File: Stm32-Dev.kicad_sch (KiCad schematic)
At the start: 1 part, among them U1 STM32F405RGTx

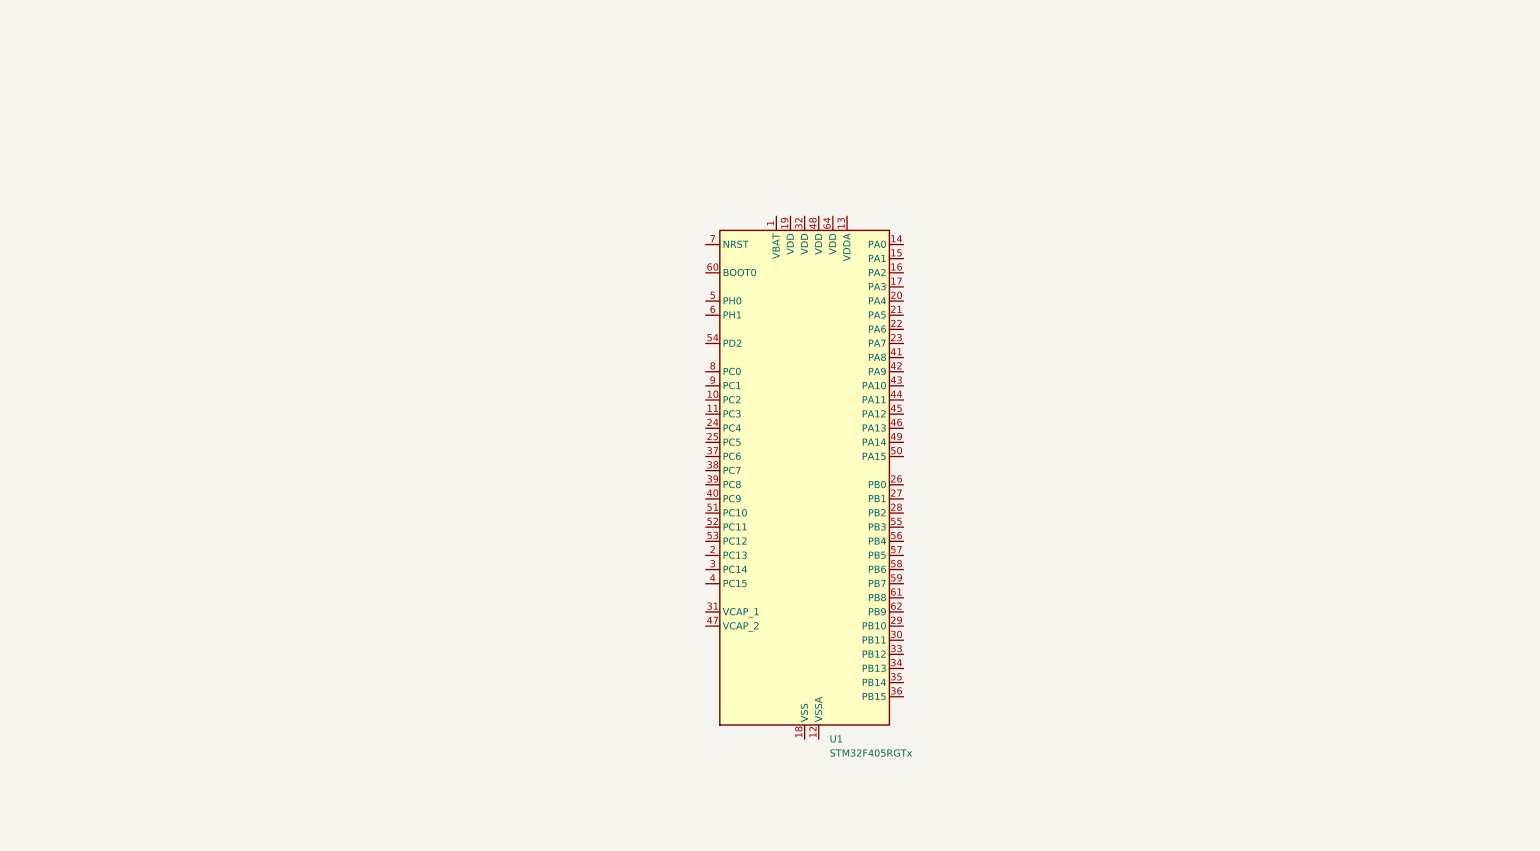
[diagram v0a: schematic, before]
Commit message: Basic MCU Setup
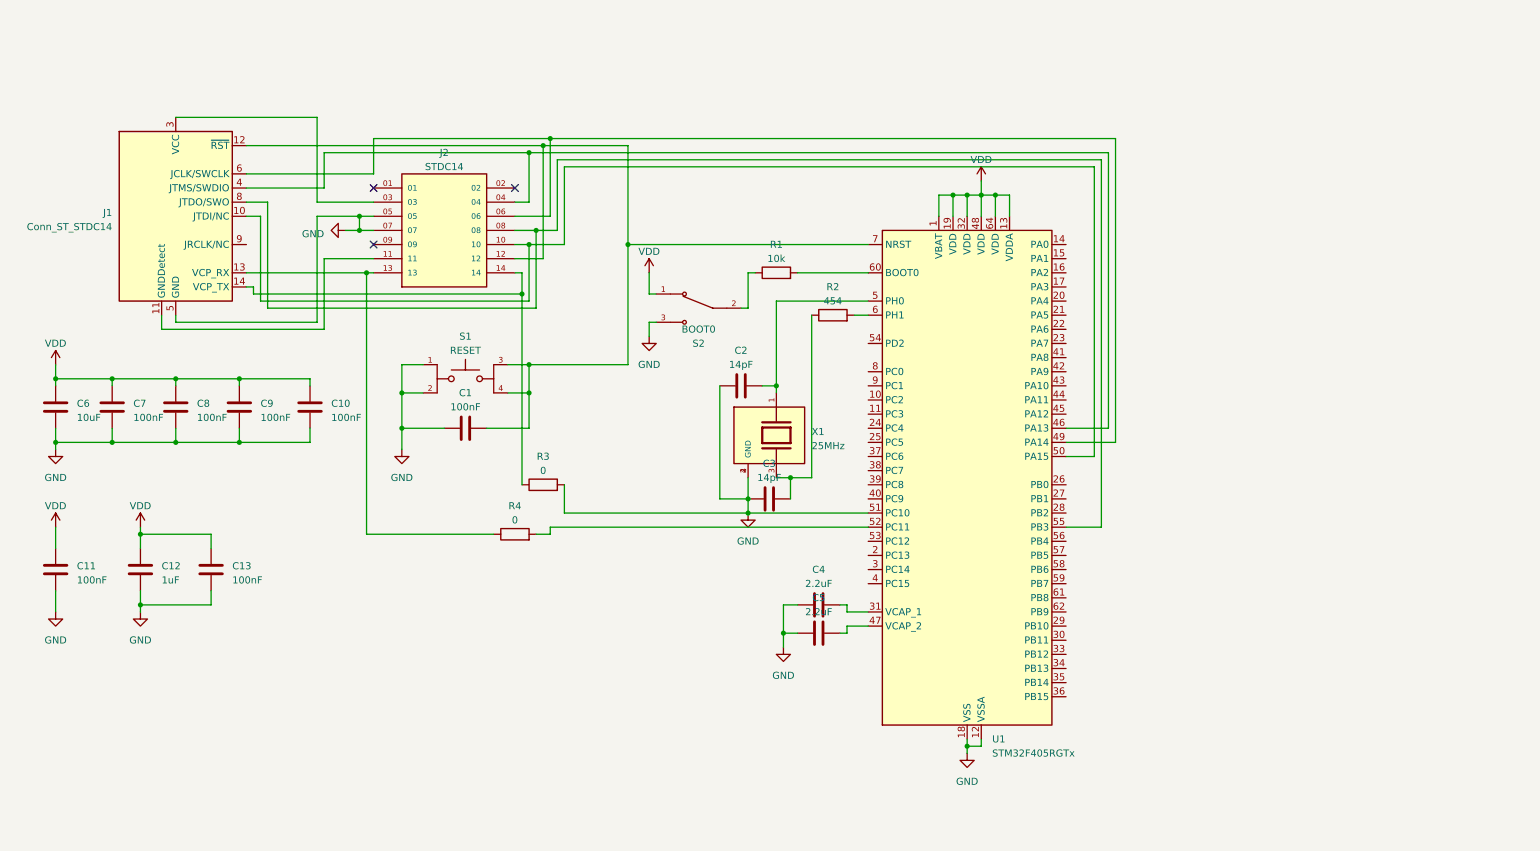
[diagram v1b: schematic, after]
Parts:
- added C1, C10, C11, C13, C7, C8, C9: 100nF, Capacitor_SMD:C_0805_2012Metric, symbol Device:C
- added C12: 1uF, Capacitor_SMD:C_0805_2012Metric, symbol Device:C
- added C2, C3: 14pF, Capacitor_SMD:C_0805_2012Metric, symbol Device:C
- added C4, C5: 2.2uF, Capacitor_SMD:C_0805_2012Metric, symbol Device:C
- added C6: 10uF, Capacitor_SMD:C_0805_2012Metric, symbol Device:C
- added J1: Conn_ST_STDC14, symbol Connector:Conn_ST_STDC14
- added J2: STDC14, SAMTEC_FTSH-107-01-L-DV-K, symbol FTSH-107-01-L-DV-K:FTSH-107-01-L-DV-K
- added R1: 10k, Resistor_SMD:R_0805_2012Metric, symbol Device:R
- added R2: 454, symbol Device:R
- added R3, R4: 0, symbol Device:R
- added S1: RESET, SW_TL3301AF160QG, symbol TL3301AF160QG:TL3301AF160QG
- added S2: BOOT0, Button_Switch_THT:SW_E-Switch_EG1224_SPDT_Angled, symbol EG1215AA:EG1215AA
- added X1: 25MHz, XTAL_ABM10W-25.0000MHZ-7-D1X-T3, symbol ABM10W-25.0000MHZ-7-D1X-T3:ABM10W-25.0000MHZ-7-D1X-T3
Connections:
- net VDD: now reaches U1.1 (VBAT)
- net VDD: now also U1.13 (VDDA), U1.19 (VDD), U1.32 (VDD), U1.48 (VDD), U1.64 (VDD), C10.1, C11.1, C12.1, C13.1, C6.1, C7.1, C8.1, C9.1, S2.1
- net GND: now reaches U1.12 (VSSA)
- net GND: now also U1.18 (VSS), U1.51 (PC10), U1.63 (VSS), C1.2, C10.2, C11.2, C12.2, C13.2, C2.2, C3.2, C4.2, C5.2, C6.2, C7.2, C8.2, C9.2, J1.5 (GND), J1.7 (GND), J2.05, J2.07, R3.2, S1.1, S1.2, S2.3, X1.2 (GND), X1.4 (GND)
- net at U1.31 (VCAP_1): now also C4.1
- net at U1.46 (PA13): now also J1.4 (JTMS/SWDIO), J2.04
- net at U1.47 (VCAP_2): now also C5.1
- net at U1.49 (PA14): now also J1.6 (JCLK/SWCLK), J2.06
- net at U1.5 (PH0): now also C2.1, X1.1
- net at U1.50 (PA15): now also J1.10 (JTDI/NC), J2.10
- net at U1.52 (PC11): now also R4.2
- net at U1.55 (PB3): now also J1.8 (JTDO/SWO), J2.08
- net at U1.6 (PH1): now also R2.2
- net at U1.60 (BOOT0): now also R1.2
- net at U1.7 (NRST): now also C1.1, J1.12 (~{RST}), J2.12, S1.3, S1.4
- new net: R1.1, S2.2
- new net: J1.14 (VCP_TX), J2.14, R3.1
- new net: C3.1, R2.1, X1.3
- new net: J1.11 (GNDDetect), J2.11
- new net: J1.13 (VCP_RX), J2.13, R4.1
- new net: J1.3 (VCC), J2.03
- no-connect marks 0 -> 3
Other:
- moved on the sheet: U1

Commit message: PCB start
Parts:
- removed J1: Conn_ST_STDC14, symbol Connector:Conn_ST_STDC14
- added H1: ~, 24_PIN_HEADER:HDRV26, symbol 24_PIN_HEADER:26_Header
- added H2: ~, 24_PIN_HEADER:HDRV25, symbol 24_PIN_HEADER:25_Header
- added R5: 0, Resistor_SMD:R_0805_2012Metric, symbol Device:R
- J2: footprint SAMTEC_FTSH-107-01-L-DV-K -> FTSH-107-01-L-DV-K:SAMTEC_FTSH-107-01-L-DV-K
- R2, R3, R4: footprint (none) -> Resistor_SMD:R_0805_2012Metric
- S1: footprint SW_TL3301AF160QG -> TL3301AF160QG:SW_TL3301AF160QG
- S2: footprint Button_Switch_THT:SW_E-Switch_EG1224_SPDT_Angled -> EG1215AA:SW_EG1215AA
- X1: footprint XTAL_ABM10W-25.0000MHZ-7-D1X-T3 -> ABM10W-25.0000MHZ-7-D1X-T3:XTAL_ABM10W-25.0000MHZ-7-D1X-T3
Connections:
- net GND: now also J2.11, H1.1; no longer R3.2, U1.51 (PC10)
- net VDD: now also R5.1
- net at U1.10 (PC2): now also H2.4
- net at U1.11 (PC3): now also H2.5
- net at U1.14 (PA0): now also H1.25
- net at U1.15 (PA1): now also H1.24
- net at U1.16 (PA2): now also H1.23
- net at U1.17 (PA3): now also H1.22
- net at U1.2 (PC13): now also H2.15
- net at U1.20 (PA4): now also H1.21
- net at U1.21 (PA5): now also H1.20
- net at U1.22 (PA6): now also H1.19
- net at U1.23 (PA7): now also H1.18
- net at U1.24 (PC4): now also H2.6
- net at U1.25 (PC5): now also H2.7
- net at U1.26 (PB0): now also H1.9
- net at U1.27 (PB1): now also H1.8
- net at U1.28 (PB2): now also H1.7
- net at U1.29 (PB10): now also H2.23
- net at U1.3 (PC14): now also H2.16
- net at U1.30 (PB11): now also H2.22
- net at U1.33 (PB12): now also H2.21
- net at U1.34 (PB13): now also H2.20
- net at U1.35 (PB14): now also H2.19
- net at U1.36 (PB15): now also H2.18
- net at U1.37 (PC6): now also H2.8
- net at U1.38 (PC7): now also H2.9
- net at U1.39 (PC8): now also H2.10
- net at U1.4 (PC15): now also H2.17
- net at U1.40 (PC9): now also H2.11
- net at U1.41 (PA8): now also H1.17
- net at U1.42 (PA9): now also H1.16
- net at U1.43 (PA10): now also H1.15
- net at U1.44 (PA11): now also H1.14
- net at U1.45 (PA12): now also H1.13
- net at J2.04, U1.46 (PA13): now also H1.12
- net at J2.06, U1.49 (PA14): now also H1.11
- net at U1.50 (PA15): now also H1.10; no longer J2.10
- net at R4.2, U1.52 (PC11): now also H2.13
- net at U1.53 (PC12): now also H2.14
- net at U1.54 (PD2): now also H2.1
- net at J2.08, U1.55 (PB3): now also H1.6
- net at U1.56 (PB4): now also H1.5
- net at U1.57 (PB5): now also H1.4
- net at U1.58 (PB6): now also H1.3
- net at U1.59 (PB7): now also H1.2
- net at U1.61 (PB8): now also H2.25
- net at U1.62 (PB9): now also H2.24
- net at U1.8 (PC0): now also H2.2
- net at U1.9 (PC1): now also H2.3
- net at J2.03: now also R5.2
- new net: H2.12, R3.2, U1.51 (PC10)
- new net +VDC: H1.26
- no-connect marks 3 -> 4
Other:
- added sheet Stm32-PowerSupply (Stm32-PowerSupply.kicad_sch)
- moved on the sheet: C1, C12, C13, C2, C3, C4, C5, J2, R1, R3, R4, S1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

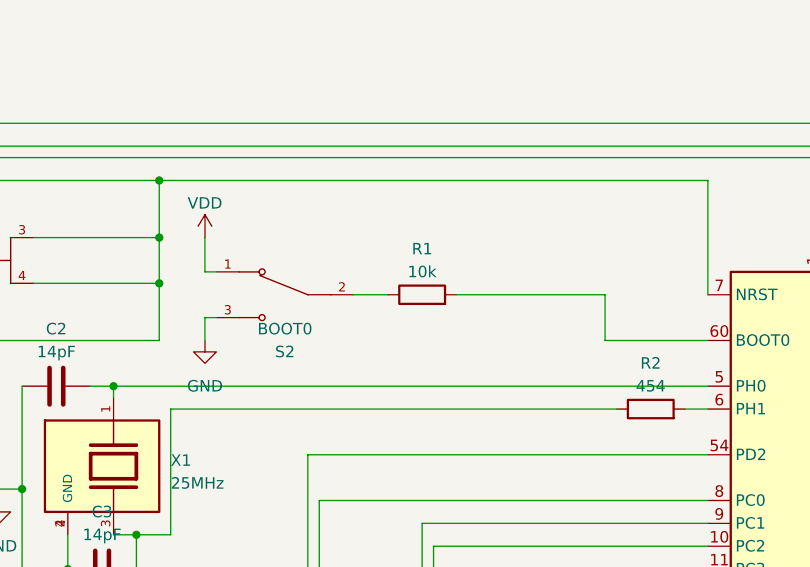
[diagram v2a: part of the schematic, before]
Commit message: Changed Boot Switch
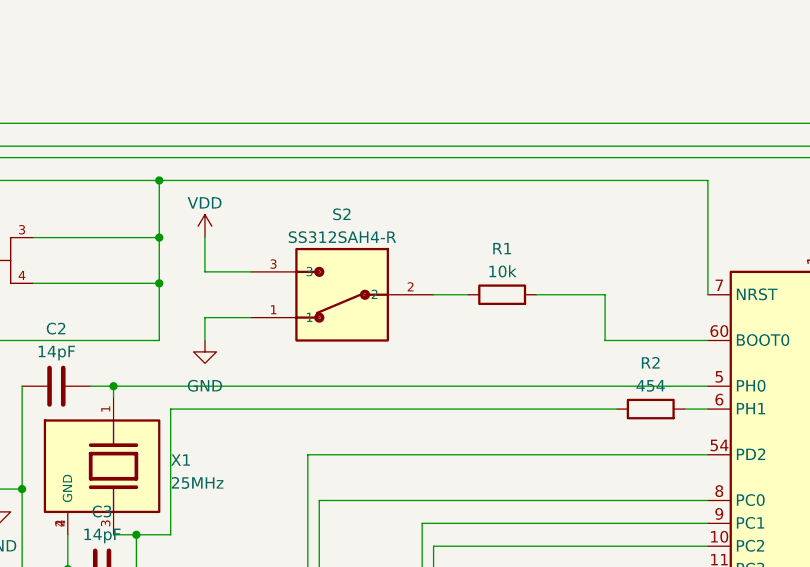
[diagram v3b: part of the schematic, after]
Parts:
- removed S2: BOOT0, EG1215AA:SW_EG1215AA, symbol EG1215AA:EG1215AA
- added S2: SS312SAH4-R, SS312SAH4-R:SW_SS312SAH4-R, symbol SS312SAH4-R:SS312SAH4-R
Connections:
- net GND: now also S2.1
- net VDD: now also S2.3
- net at R1.1: now also S2.2
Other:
- moved on the sheet: R1
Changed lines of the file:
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@@
+    (stroke (width 0) (type default))
+  )
+  (wire (pts (xy 110.49 52.07) (xy 115.57 52.07))
     (stroke (width 0) (type default))
   )
@@
     (stroke (width 0) (type default))
   )
-  (wire (pts (xy 138.43 54.61) (xy 154.94 54.61))
+  (wire (pts (xy 147.32 54.61) (xy 154.94 54.61))
     (stroke (width 0) (type default))
   )
@@
     (stroke (width 0) (type default))
   )
-  (wire (pts (xy 127 54.61) (xy 130.81 54.61))
-    (stroke (width 0) (type default))
-  )
-  (wire (pts (xy 110.49 52.07) (xy 111.76 52.07))
-    (stroke (width 0) (type default))
-  )
   (wire (pts (xy 201.93 105.41) (xy 208.28 105.41))
     (stroke (width 0) (type default))
@@
     (stroke (width 0) (type default))
   )
-  (wire (pts (xy 110.49 57.15) (xy 111.76 57.15))
-    (stroke (width 0) (type default))
-  )
   (wire (pts (xy 87.63 76.2) (xy 90.17 76.2))
     (stroke (width 0) (type default))
@@
     (stroke (width 0) (type default))
   )
+  (wire (pts (xy 135.89 54.61) (xy 139.7 54.61))
+    (stroke (width 0) (type default))
+  )
   (wire (pts (xy 238.76 115.57) (xy 240.03 115.57))
     (stroke (width 0) (type default))
@@
     (stroke (width 0) (type default))
   )
+  (wire (pts (xy 110.49 57.15) (xy 115.57 57.15))
+    (stroke (width 0) (type default))
+  )
   (wire (pts (xy 137.16 85.09) (xy 137.16 110.49))
     (stroke (width 0) (type default))
@@
     )
   )
-  (symbol (lib_id "Device:R") (at 134.62 54.61 90) (unit 1)
-    (in_bom yes) (on_board yes) (dnp no) (fields_autoplaced)
-    (property "Reference" "R1" (at 134.62 49.53 90)
-      (effects (font (size 1.27 1.27)))
-    )
-    (property "Value" "10k" (at 134.62 52.07 90)
-      (effects (font (size 1.27 1.27)))
-    )
-    (property "Footprint" "Resistor_SMD:R_0805_2012Metric" (at 134.62 56.388 90)
-      (effects (font (size 1.27 1.27)) hide)
-    )
-    (property "Datasheet" "~" (at 134.62 54.61 0)
+  (symbol (lib_id "Device:R") (at 143.51 54.61 90) (unit 1)
+    (in_bom yes) (on_board yes) (dnp no) (fields_autoplaced)
+    (property "Reference" "R1" (at 143.51 49.53 90)
+      (effects (font (size 1.27 1.27)))
+    )
+    (property "Value" "10k" (at 143.51 52.07 90)
+      (effects (font (size 1.27 1.27)))
+    )
+    (property "Footprint" "Resistor_SMD:R_0805_2012Metric" (at 143.51 56.388 90)
+      (effects (font (size 1.27 1.27)) hide)
+    )
+    (property "Datasheet" "~" (at 143.51 54.61 0)
       (effects (font (size 1.27 1.27)) hide)
     )
@@
     )
   )
-  (symbol (lib_id "EG1215AA:EG1215AA") (at 119.38 54.61 0) (mirror y) (unit 1)
-    (in_bom yes) (on_board yes) (dnp no)
-    (property "Reference" "S2" (at 119.38 60.96 0)
-      (effects (font (size 1.27 1.27)))
-    )
-    (property "Value" "BOOT0" (at 119.38 58.42 0)
-      (effects (font (size 1.27 1.27)))
-    )
-    (property "Footprint" "EG1215AA:SW_EG1215AA" (at 119.38 54.61 0)
+  (symbol (lib_id "SS312SAH4-R:SS312SAH4-R") (at 125.73 54.61 180) (unit 1)
+    (in_bom yes) (on_board yes) (dnp no) (fields_autoplaced)
+    (property "Reference" "S2" (at 125.73 45.72 0)
+      (effects (font (size 1.27 1.27)))
+    )
+    (property "Value" "SS312SAH4-R" (at 125.73 48.26 0)
+      (effects (font (size 1.27 1.27)))
+    )
+    (property "Footprint" "SS312SAH4-R:SW_SS312SAH4-R" (at 125.73 54.61 0)
       (effects (font (size 1.27 1.27)) (justify bottom) hide)
     )
-    (property "Datasheet" "" (at 119.38 54.61 0)
-      (effects (font (size 1.27 1.27)) hide)
-    )
-    (property "PARTREV" "A" (at 119.38 54.61 0)
+    (property "Datasheet" "" (at 125.73 54.61 0)
+      (effects (font (size 1.27 1.27)) hide)
+    )
+    (property "MANUFACTURER" "NKK switches" (at 125.73 54.61 0)
       (effects (font (size 1.27 1.27)) (justify bottom) hide)
     )
-    (property "STANDARD" "Manufacturer Recommendations" (at 119.38 54.61 0)
-      (effects (font (size 1.27 1.27)) (justify bottom) hide)
-    )
-    (property "MAXIMUM_PACKAGE_HEIGHT" "1.40mm" (at 119.38 54.61 0)
-      (effects (font (size 1.27 1.27)) (justify bottom) hide)
-    )
-    (property "MANUFACTURER" "E Switch" (at 119.38 54.61 0)
-      (effects (font (size 1.27 1.27)) (justify bottom) hide)
-    )

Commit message: First Test Board
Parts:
- removed H1: ~, 24_PIN_HEADER:HDRV26, symbol 24_PIN_HEADER:26_Header
- removed H2: ~, 24_PIN_HEADER:HDRV25, symbol 24_PIN_HEADER:25_Header
- added H1, H2: ~, 24_PIN_HEADER:HDRV16, symbol 24_PIN_HEADER:16_Header
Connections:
- net +VDC: now also H2.16
- net GND: now also H2.1
- net at U1.10 (PC2): now also H1.4
- net at U1.11 (PC3): now also H1.5
- net at U1.14 (PA0): now also H2.14
- net at U1.15 (PA1): now also H2.13
- net at U1.16 (PA2): now also H2.12
- net at U1.17 (PA3): now also H2.11
- net at U1.20 (PA4): now also H2.10
- net at U1.21 (PA5): now also H2.9
- net at U1.22 (PA6): now also H2.8
- net at U1.29 (PB10): now also H1.16
- net at U1.30 (PB11): now also H1.15
- net at U1.33 (PB12): now also H1.14
- net at U1.34 (PB13): now also H1.13
- net at U1.35 (PB14): now also H1.12
- net at U1.37 (PC6): now also H1.6
- net at U1.38 (PC7): now also H1.7
- net at U1.39 (PC8): now also H1.8
- net at U1.41 (PA8): now also H2.7
- net at U1.42 (PA9): now also H2.6
- net at U1.43 (PA10): now also H2.5
- net at U1.44 (PA11): now also H2.4
- net at R3.2, U1.51 (PC10): now also H1.9
- net at R4.2, U1.52 (PC11): now also H1.10
- net at U1.53 (PC12): now also H1.11
- net at U1.54 (PD2): now also H1.1
- net at U1.58 (PB6): now also H2.3
- net at U1.59 (PB7): now also H2.2
- net at U1.8 (PC0): now also H1.2
- net at U1.9 (PC1): now also H1.3
